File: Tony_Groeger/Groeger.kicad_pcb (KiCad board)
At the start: 2 copper layers, 38 x 38 mm, 14 parts, among them P1 EBUS, P2 RS232, Q1 PN2222A, U1 7805, U2 4011

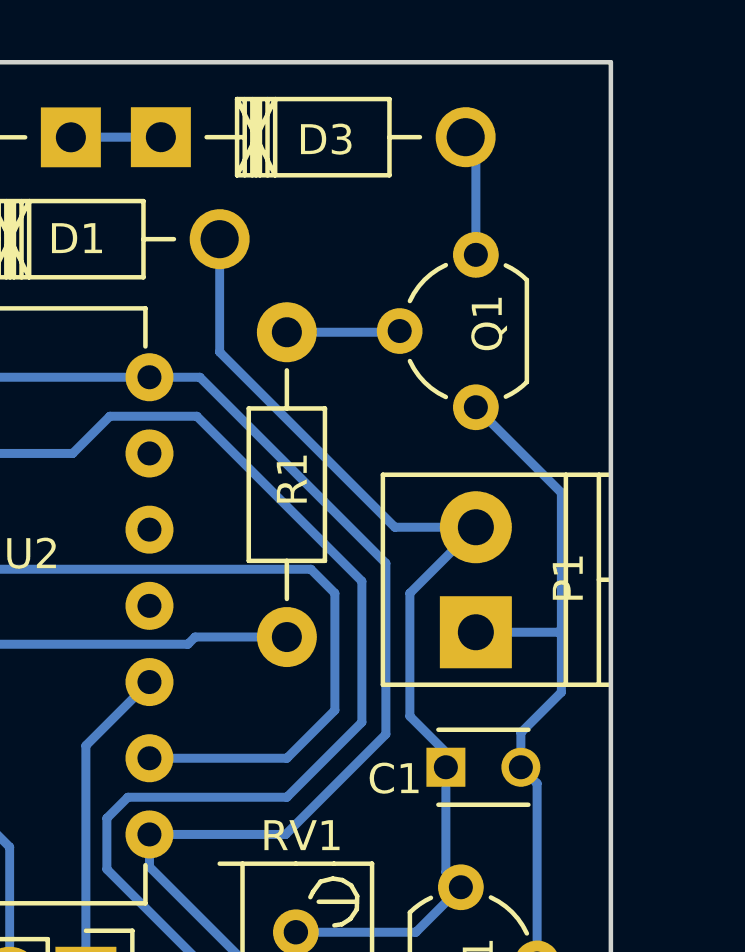
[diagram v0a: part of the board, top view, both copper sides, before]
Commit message: Changed Groeger's PCB terminal block component to something we have on hand.
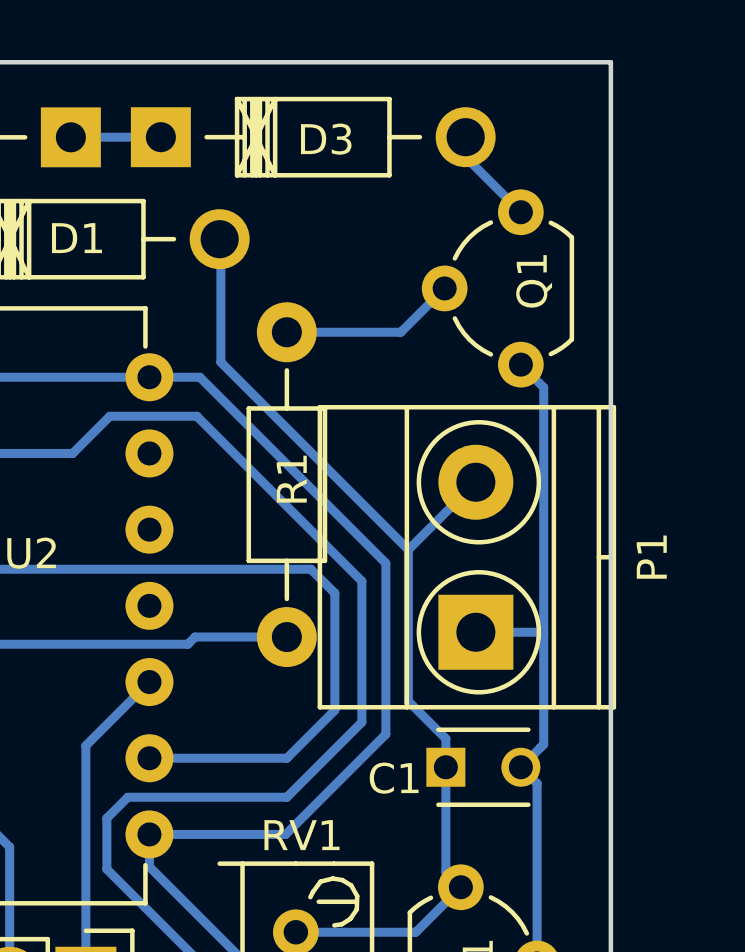
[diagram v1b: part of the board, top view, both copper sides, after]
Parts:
- P1: footprint Terminal_Blocks:TerminalBlock_Pheonix_PT-3.5mm_2pol -> Terminal_Blocks:TerminalBlock_Pheonix_MKDS1.5-2pol
- moved Q1 2.07 mm to (47.0, 22.1)
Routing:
- net Net-(Q1-Pad2): track 3.78 -> 5.86 mm
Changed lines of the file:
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@@
   (general
     (links 27)
-    (no_connects 0)
-    (area 11.924999 11.775 50.425001 50.075001)
+    (no_connects 1)
+    (area 11.924999 11.775 52.375 50.075001)
     (thickness 1.6)
     (drawings 4)
-    (tracks 81)
+    (tracks 82)
     (zones 0)
     (modules 14)
@@
     (visible_elements FFFFFF7F)
     (pcbplotparams
-      (layerselection 0x00000_80000000)
+      (layerselection 0x010f0_80000001)
       (usegerberextensions false)
       (excludeedgelayer true)
@@
       (padsonsilk false)
       (subtractmaskfromsilk false)
-      (outputformat 4)
+      (outputformat 1)
       (mirror false)
-      (drillshape 1)
+      (drillshape 0)
       (scaleselection 1)
       (outputdirectory gerbers))
@@
     (add_net VDD)
   )
+  (module Terminal_Blocks:TerminalBlock_Pheonix_MKDS1.5-2pol (layer F.Cu)
+    (at 45.5 31 90)
+    (descr "2-way 5mm pitch terminal block, Phoenix MKDS series")
+    (fp_text reference P1 (at 2.5 5.9 90) (layer F.SilkS)
+      (effects (font (size 1 1) (thickness 0.15)))
+    )
+    (fp_text value EBUS (at 2.5 -6.6 90) (layer F.Fab)
+      (effects (font (size 1 1) (thickness 0.15)))
+    )
+    (fp_line (start -2.7 -5.4) (end 7.7 -5.4) (layer F.CrtYd) (width 0.05))
+    (fp_line (start -2.7 4.8) (end -2.7 -5.4) (layer F.CrtYd) (width 0.05))
+    (fp_line (start 7.7 4.8) (end -2.7 4.8) (layer F.CrtYd) (width 0.05))
+    (fp_line (start 7.7 -5.4) (end 7.7 4.8) (layer F.CrtYd) (width 0.05))
+    (fp_line (start 2.5 4.1) (end 2.5 4.6) (layer F.SilkS) (width 0.15))
+    (fp_circle (center 5 0.1) (end 3 0.1) (layer F.SilkS) (width 0.15))
+    (fp_circle (center 0 0.1) (end 2 0.1) (layer F.SilkS) (width 0.15))
+    (fp_line (start -2.5 2.6) (end 7.5 2.6) (layer F.SilkS) (width 0.15))
+    (fp_line (start -2.5 -2.3) (end 7.5 -2.3) (layer F.SilkS) (width 0.15))
+    (fp_line (start -2.5 4.1) (end 7.5 4.1) (layer F.SilkS) (width 0.15))
+    (fp_line (start -2.5 4.6) (end 7.5 4.6) (layer F.SilkS) (width 0.15))
+    (fp_line (start 7.5 4.6) (end 7.5 -5.2) (layer F.SilkS) (width 0.15))
+    (fp_line (start 7.5 -5.2) (end -2.5 -5.2) (layer F.SilkS) (width 0.15))
+    (fp_line (start -2.5 -5.2) (end -2.5 4.6) (layer F.SilkS) (width 0.15))
+    (pad 1 thru_hole rect (at 0 0 90) (size 2.5 2.5) (drill 1.3) (layers *.Cu *.Mask F.SilkS)
+      (net 2 EBUS-))
+    (pad 2 thru_hole circle (at 5 0 90) (size 2.5 2.5) (drill 1.3) (layers *.Cu *.Mask F.SilkS)
+      (net 1 EBUS+))
+    (model Terminal_Blocks.3dshapes/TerminalBlock_Pheonix_MKDS1.5-2pol.wrl
+      (at (xyz 0.0984 0 0))
+      (scale (xyz 1 1 1))
+      (rotate (xyz 0 0 0))
+    )
+  )
   (module Diodes_ThroughHole:Diode_DO-41_SOD81_Horizontal_RM10 (layer F.Cu)
     (at 26.8 17.9)
@@
     )
   )
-  (module Terminal_Blocks:TerminalBlock_Pheonix_PT-3.5mm_2pol (layer F.Cu)
-    (at 45.5 31 90)
-    (descr "2-way 3.5mm pitch terminal block, Phoenix PT series")
-    (fp_text reference P1 (at 1.8 3.1 90) (layer F.SilkS)
-      (effects (font (size 1 1) (thickness 0.15)))
-    )
-    (fp_text value EBUS (at 1.6 -2.1 90) (layer F.Fab)
-      (effects (font (size 1 1) (thickness 0.15)))
-    )
-    (fp_line (start -1.9 -3.3) (end 5.4 -3.3) (layer F.CrtYd) (width 0.05))
-    (fp_line (start -1.9 4.7) (end -1.9 -3.3) (layer F.CrtYd) (width 0.05))
-    (fp_line (start 5.4 4.7) (end -1.9 4.7) (layer F.CrtYd) (width 0.05))
-    (fp_line (start 5.4 -3.3) (end 5.4 4.7) (layer F.CrtYd) (width 0.05))
-    (fp_line (start 1.75 4.1) (end 1.75 4.5) (layer F.SilkS) (width 0.15))
-    (fp_line (start -1.75 3) (end 5.25 3) (layer F.SilkS) (width 0.15))
-    (fp_line (start -1.75 4.1) (end 5.25 4.1) (layer F.SilkS) (width 0.15))
-    (fp_line (start -1.75 -3.1) (end -1.75 4.5) (layer F.SilkS) (width 0.15))
-    (fp_line (start 5.25 4.5) (end 5.25 -3.1) (layer F.SilkS) (width 0.15))
-    (fp_line (start 5.25 -3.1) (end -1.75 -3.1) (layer F.SilkS) (width 0.15))
-    (pad 2 thru_hole circle (at 3.5 0 90) (size 2.4 2.4) (drill 1.2) (layers *.Cu *.Mask F.SilkS)
-      (net 1 EBUS+))
-    (pad 1 thru_hole rect (at 0 0 90) (size 2.4 2.4) (drill 1.2) (layers *.Cu *.Mask F.SilkS)
-      (net 2 EBUS-))
-    (model Terminal_Blocks.3dshapes/TerminalBlock_Pheonix_PT-3.5mm_2pol.wrl
-      (at (xyz 0 0 0))
-      (scale (xyz 1 1 1))
-      (rotate (xyz 0 0 0))
-    )
-  )
   (module Pin_Headers:Pin_Header_Straight_1x02 (layer F.Cu)
     (at 32.5 42.5 270)
@@
   )
   (module TO_SOT_Packages_THT:TO-92_Molded_Wide (layer F.Cu)
-    (at 45.5 23.5 90)
+    (at 47 22.08 90)
     (descr "TO-92 leads molded, wide, drill 0.8mm (see NXP sot054_po.pdf)")
     (tags "to-92 sc-43 sc-43a sot54 PA33 transistor")
@@
   (gr_line (start 50 12) (end 50 50) (angle 90) (layer Edge.Cuts) (width 0.15))
   (gr_line (start 12 12) (end 50 12) (angle 90) (layer Edge.Cuts) (width 0.15))
-  (segment (start 36.96 17.89746) (end 36.96 21.66) (width 0.3) (layer B.Cu) (net 1))
-  (segment (start 42.8 27.5) (end 45.5 27.5) (width 0.3) (layer B.Cu) (net 1))
-  (segment (start 36.96 21.66) (end 42.8 27.5) (width 0.3) (layer B.Cu) (net 1))
+  (segment (start 45.5 26) (end 43.25 28.25) (width 0.3) (layer B.Cu) (net 1))
+  (segment (start 44.5 35.5) (end 44.5 34.55) (width 0.3) (layer B.Cu) (net 1))
+  (segment (start 44.5 34.55) (end 43.25 33.3) (width 0.3) (layer B.Cu) (net 1))
+  (segment (start 43.25 33.3) (end 43.25 28.25) (width 0.3) (layer B.Cu) (net 1))
+  (segment (start 37 22) (end 37 17.93746) (width 0.3) (layer B.Cu) (net 1))
+  (segment (start 43.25 28.25) (end 37 22) (width 0.3) (layer B.Cu) (net 1))
+  (segment (start 37 17.93746) (end 36.96 17.89746) (width 0.3) (layer B.Cu) (net 1))
   (segment (start 44.5 35.5) (end 44.5 35) (width 0.3) (layer B.Cu) (net 1))
-  (segment (start 44.5 35) (end 43.3 33.8) (width 0.3) (layer B.Cu) (net 1))
-  (segment (start 43.3 29.7) (end 45.5 27.5) (width 0.3) (layer B.Cu) (net 1))
-  (segment (start 43.3 33.8) (end 43.3 29.7) (width 0.3) (layer B.Cu) (net 1))
   (segment (start 44.5 35.5) (end 44.5 39) (width 0.3) (layer B.Cu) (net 1))
   (segment (start 44.5 39) (end 45 39.5) (width 0.3) (layer B.Cu) (net 1))
   (segment (start 39.5 41) (end 43.5 41) (width 0.3) (layer B.Cu) (net 1))
   (segment (start 43.5 41) (end 45 39.5) (width 0.3) (layer B.Cu) (net 1))
-  (segment (start 45.5 31) (end 48.25 31) (width 0.3) (layer B.Cu) (net 2))
-  (segment (start 48.25 31) (end 48.35 30.9) (width 0.3) (layer B.Cu) (net 2))
-  (segment (start 47 35.5) (end 47 34.35) (width 0.3) (layer B.Cu) (net 2))
-  (segment (start 48.35 26.35) (end 45.5 23.5) (width 0.3) (layer B.Cu) (net 2))
-  (segment (start 48.35 33) (end 48.35 30.9) (width 0.3) (layer B.Cu) (net 2))
-  (segment (start 48.35 30.9) (end 48.35 26.35) (width 0.3) (layer B.Cu) (net 2))
-  (segment (start 47 34.35) (end 48.35 33) (width 0.3) (layer B.Cu) (net 2))
+  (segment (start 47.761999 22.841999) (end 47.761999 31) (width 0.3) (layer B.Cu) (net 2))
+  (segment (start 47.761999 31) (end 47.761999 34.738001) (width 0.3) (layer B.Cu) (net 2))
+  (segment (start 45.5 31) (end 47.761999 31) (width 0.3) (layer B.Cu) (net 2))
+  (segment (start 47 22.08) (end 47.761999 22.841999) (width 0.3) (layer B.Cu) (net 2))
+  (segment (start 47.761999 34.738001) (end 47.649999 34.850001) (width 0.3) (layer B.Cu) (net 2))
+  (segment (start 47.649999 34.850001) (end 47 35.5) (width 0.3) (layer B.Cu) (net 2))
   (segment (start 27 37.74) (end 27 48) (width 0.3) (layer B.Cu) (net 2))
   (segment (start 39.5 46.08) (end 39.5 48) (width 0.3) (layer B.Cu) (net 2))
@@
   (segment (start 35 14.49746) (end 32.00508 14.49746) (width 0.3) (layer B.Cu) (net 5))
   (segment (start 32.00508 14.49746) (end 32 14.50254) (width 0.3) (layer B.Cu) (net 5))
-  (segment (start 45.5 18.42) (end 45.5 14.83746) (width 0.3) (layer B.Cu) (net 6))
+  (segment (start 47 17) (end 45.16 15.16) (width 0.3) (layer B.Cu) (net 6))
+  (segment (start 45.16 15.16) (end 45.16 14.49746) (width 0.3) (layer B.Cu) (net 6))
   (segment (start 45.5 14.83746) (end 45.16 14.49746) (width 0.3) (layer B.Cu) (net 6))
   (segment (start 17.5 30) (end 17.5 33.5) (width 0.3) (layer B.Cu) (net 7))
@@
   (segment (start 29.96 42.5) (end 29.96 38.16) (width 0.3) (layer B.Cu) (net 9))
   (segment (start 29.96 38.16) (end 27 35.2) (width 0.3) (layer B.Cu) (net 9))
-  (segment (start 39.2 21) (end 42.92 21) (width 0.3) (layer B.Cu) (net 10))
-  (segment (start 42.92 21) (end 42.96 20.96) (width 0.3) (layer B.Cu) (net 10))
+  (segment (start 39.2 21) (end 43 21) (width 0.3) (layer B.Cu) (net 10))
+  (segment (start 43 21) (end 44.46 19.54) (width 0.3) (layer B.Cu) (net 10))
   (segment (start 39.2 31.16) (end 36.14 31.16) (width 0.3) (layer B.Cu) (net 11))
   (segment (start 28.28 31.4) (end 27 30.12) (width 0.3) (layer B.Cu) (net 11))

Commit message: Added some text on the copper layer.
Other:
- board text added: "eBUS Adapter"
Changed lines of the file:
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@@
   (general
     (links 27)
-    (no_connects 1)
+    (no_connects 0)
     (area 11.924999 11.775 52.375 50.075001)
     (thickness 1.6)
-    (drawings 4)
+    (drawings 5)
     (tracks 82)
     (zones 0)
@@
     )
   )
+  (gr_text "eBUS\nAdapter" (at 18 20) (layer B.Cu)
+    (effects (font (size 1.5 1.5) (thickness 0.3)) (justify mirror))
+  )
   (gr_line (start 12 50) (end 12 12) (angle 90) (layer Edge.Cuts) (width 0.15))
